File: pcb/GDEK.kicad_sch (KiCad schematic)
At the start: 324 parts, among them J1 TYPE-C-31-M-13C, J101 TYPE-C-31-M-13C, J102 AudioJack4, J2 AudioJack4, SW1 SW_Push_45deg, SW10 SW_Push_45deg, SW101 SW_Push_45deg, SW102 SW_Push_45deg, SW103 SW_Push_45deg, SW104 SW_Push_45deg, SW105 SW_Push_45deg, SW106 SW_Push_45deg, SW107 SW_Push_45deg, SW108 SW_Push_45deg, SW109 SW_Push_45deg, SW11 SW_Push_45deg, SW110 SW_Push_45deg, SW111 SW_Push_45deg, SW112 SW_Push_45deg, SW113 SW_Push_45deg, SW114 SW_Push_45deg, SW115 SW_Push_45deg, SW116 SW_Push_45deg, SW117 SW_Push_45deg, SW118 SW_Push_45deg, SW119 SW_Push_45deg, SW12 SW_Push_45deg, SW120 SW_Push_45deg, SW121 SW_Push_45deg, SW122 SW_Push_45deg, SW123 SW_Push_45deg, SW124 SW_Push_45deg, SW125 SW_Push_45deg, SW126 SW_Push_45deg, SW127 SW_Push_45deg, SW128 SW_Push_45deg, SW129 SW_Push_45deg, SW13 SW_Push_45deg, SW130 SW_Push_45deg, SW131 RotaryEncoder_Switch, SW14 SW_Push_45deg, SW15 SW_Push_45deg, SW16 SW_Push_45deg, SW17 SW_Push_45deg, SW18 SW_Push_45deg, SW19 SW_Push_45deg, SW2 SW_Push_45deg, SW20 SW_Push_45deg, SW21 SW_Push_45deg, SW22 SW_Push_45deg, SW23 SW_Push_45deg, SW24 SW_Push_45deg, SW25 SW_Push_45deg, SW26 SW_Push_45deg, SW27 SW_Push_45deg, SW28 SW_Push_45deg, SW29 SW_Push_45deg, SW3 SW_Push_45deg, SW30 SW_Push_45deg, SW31 RotaryEncoder_Switch, SW4 SW_Push_45deg, SW5 SW_Push_45deg, SW6 SW_Push_45deg, SW7 SW_Push_45deg, SW8 SW_Push_45deg, SW9 SW_Push_45deg, U1 RP2040, U101 RP2040, U102 W25Q128JVS, U103 74AHCT1G125, U104 USBLC6-2P6, U105 XC6210B332MR, U2 W25Q128JVS, U3 74AHCT1G125, U4 USBLC6-2P6, U5 XC6210B332MR, Y1 ABM8-272-T3, Y101 ABM8-272-T3

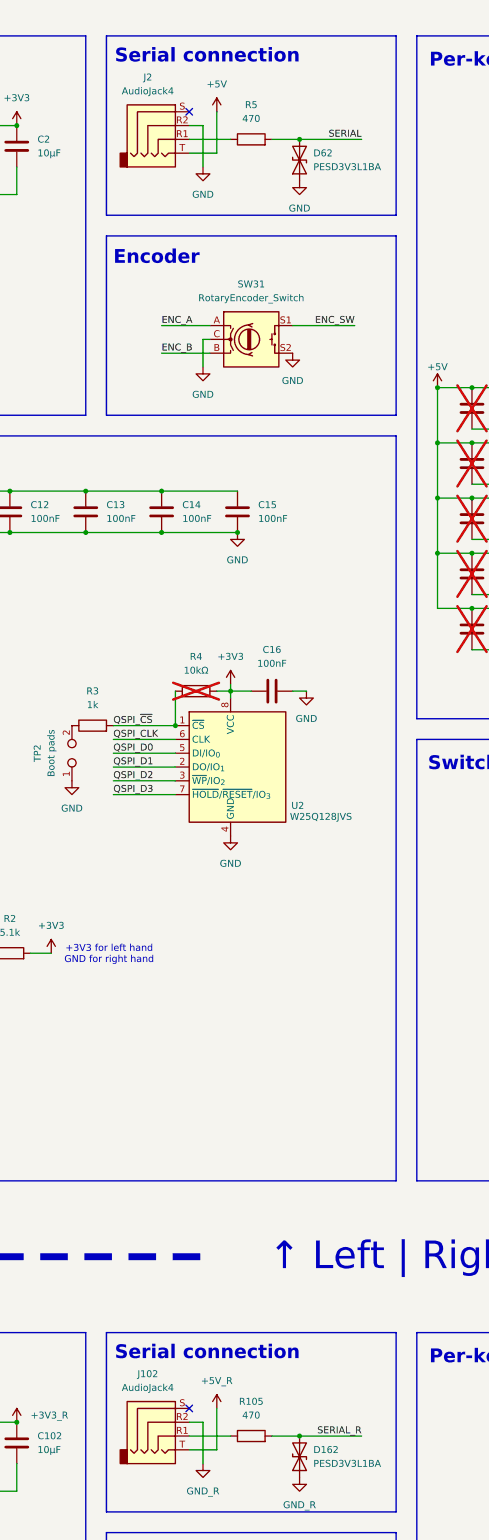
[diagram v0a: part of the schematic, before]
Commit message: 🔥 Remove protection resistor on serial line
This prevents communication between halves because of the high impedance of the MCU’s GPIO which makes a low level at a voltage too high to be registered as low.
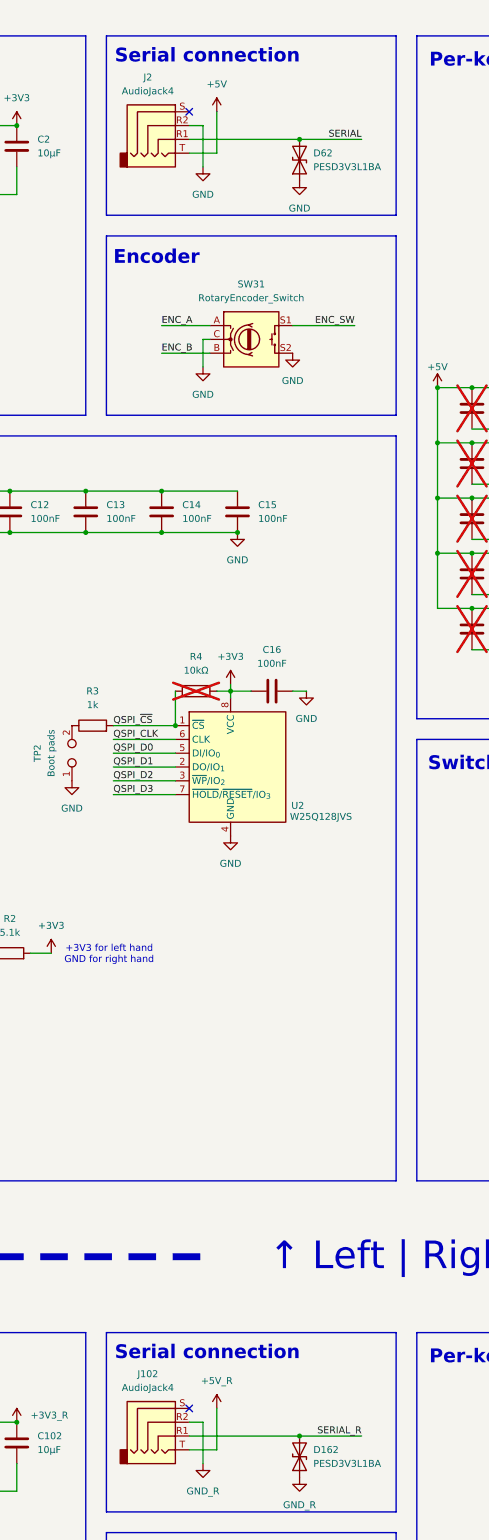
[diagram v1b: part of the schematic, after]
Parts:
- removed R105, R5: 470, Resistor_SMD:R_0402_1005Metric, symbol Device:R
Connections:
- net SERIAL: now also J2.R1
- net SERIAL_R: now also J102.R1
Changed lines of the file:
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@@
 	(wire
 		(pts
-			(xy 168.91 279.4) (xy 176.53 279.4)
+			(xy 168.91 279.4) (xy 189.23 279.4)
 		)
 		(stroke
@@
 	(wire
 		(pts
-			(xy 184.15 40.64) (xy 189.23 40.64)
-		)
-		(stroke
-			(width 0)
-			(type default)
-		)
-	)
-	(wire
-		(pts
 			(xy 168.91 38.1) (xy 171.45 38.1)
 		)
@@
 	(wire
 		(pts
-			(xy 184.15 279.4) (xy 189.23 279.4)
-		)
-		(stroke
-			(width 0)
-			(type default)
-		)
-	)
-	(wire
-		(pts
 			(xy 111.76 175.26) (xy 128.27 175.26)
 		)
@@
 	(wire
 		(pts
-			(xy 168.91 40.64) (xy 176.53 40.64)
+			(xy 168.91 40.64) (xy 189.23 40.64)
 		)
 		(stroke
@@
 	)
 	(symbol
-		(lib_id "Device:R")
-		(at 180.34 40.64 90)
-		(unit 1)
-		(exclude_from_sim no)
-		(in_bom yes)
-		(on_board yes)
-		(dnp no)
-		(fields_autoplaced yes)
-		(property "Reference" "R5"
-			(at 180.34 34.29 90)
-			(effects
-				(font
-					(size 1.27 1.27)
-				)
-			)
-		)
-		(property "Value" "470"
-			(at 180.34 36.83 90)
-			(effects
-				(font
-					(size 1.27 1.27)
-				)
-			)
-		)
-		(property "Footprint" "Resistor_SMD:R_0402_1005Metric"
-			(at 180.34 42.418 90)
-			(effects
-				(font
-					(size 1.27 1.27)
-				)
-				(hide yes)
-			)
-		)
-		(property "Datasheet" "~"
-			(at 180.34 40.64 0)
-			(effects
-				(font
-					(size 1.27 1.27)
-				)
-				(hide yes)
-			)
-		)
-		(property "Description" "Resistor"
-			(at 180.34 40.64 0)
-			(effects
-				(font
-					(size 1.27 1.27)
-				)
-				(hide yes)
-			)
-		)
-		(property "LCSC" "C25117"
-			(at 180.34 40.64 90)
-			(effects
-				(font
-					(size 1.27 1.27)
-				)
-				(hide yes)
-			)
-		)
-		(pin "1"
-		)
-		(pin "2"
-		)
-		(instances
-			(project ""
-				(path "/c27e6219-942d-4ad4-b4df-18894276b69d"
-					(reference "R5")
-					(unit 1)
-				)
-			)
-		)
-	)
-	(symbol
 		(lib_id "power:GND")
 		(at 284.48 35.56 180)
@@
 					(unit 1)
 				)
-			)
-		)
-	)
-	(symbol
-		(lib_id "Device:R")
-		(at 180.34 279.4 90)
-		(unit 1)
-		(exclude_from_sim no)
-		(in_bom yes)
-		(on_board yes)
-		(dnp no)
-		(fields_autoplaced yes)
-		(property "Reference" "R105"
-			(at 180.34 273.05 90)
-			(effects
-				(font
-					(size 1.27 1.27)
-				)
-			)
-		)
-		(property "Value" "470"
-			(at 180.34 275.59 90)
-			(effects
-				(font
-					(size 1.27 1.27)
-				)
-			)
-		)
-		(property "Footprint" "Resistor_SMD:R_0402_1005Metric"
-			(at 180.34 281.178 90)
-			(effects
-				(font
-					(size 1.27 1.27)
-				)
-				(hide yes)
-			)
-		)
-		(property "Datasheet" "~"
-			(at 180.34 279.4 0)
-			(effects
-				(font
-					(size 1.27 1.27)
-				)
-				(hide yes)
-			)
-		)
-		(property "Description" "Resistor"
-			(at 180.34 279.4 0)
-			(effects
-				(font
-					(size 1.27 1.27)
-				)
-				(hide yes)
-			)
-		)
-		(property "LCSC" "C25117"
-			(at 180.34 279.4 90)
-			(effects
-				(font
-					(size 1.27 1.27)
-				)
-				(hide yes)
-			)
-		)
-		(pin "1"
-		)
-		(pin "2"
-		)
-		(instances
-			(project "GDEK"
-				(path "/c27e6219-942d-4ad4-b4df-18894276b69d"
-					(reference "R105")
-					(unit 1)
-				)

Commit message: ♻️ Put the encoders’ switches on the matrix
Required if I want to be able to remap it using VIA or Vial. Yeah it’s a bummer…
Also fixed all DRC issues (updated standard footprints and reduced courtyard’s size of SK6812MINI-E because of the slightly bigger switches’ holes).
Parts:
- added D131, D31: D_Small, Diode_SMD:D_SOD-123, symbol Device:D_Small
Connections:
- net GND: no longer SW31.S2
- net GND_R: no longer SW131.S2
- net ROW4: now also D31.1 (K)
- net ROW4_R: now also D131.1 (K)
- net ENC_SW renamed COL6
- net ENC_SW_R renamed COL6_R
- net COL6_R: now also SW131.S2; no longer SW131.S1
- new net ENC_SW_OUT: D31.2 (A), SW31.S2
- new net ENC_SW_OUT_R: D131.2 (A), SW131.S1
